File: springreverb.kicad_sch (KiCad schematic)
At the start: 53 parts, among them J1 IN, J10 From_Tank, J11 From2, J12 From, J13 VR2_3, J14 OUT, J2 GND2, J3 GND, J4 Vin, J5 VR1_3, J6 VR1_2, J7 To, J8 To2, J9 To_Tank, U1 TL072, U2 TC1044S, U3 4556ADD

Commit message: 配置修整
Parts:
- added R14, R15: 10, Resistor_THT:R_Axial_DIN0204_L3.6mm_D1.6mm_P7.62mm_Horizontal, symbol Device:R_Small
- J2: value GND2 -> VR1_1
- R10: value 10 -> 47
- R12: footprint Resistor_THT:R_Axial_DIN0204_L3.6mm_D1.6mm_P7.62mm_Horizontal -> Resistor_THT:R_Axial_DIN0204_L3.6mm_D1.6mm_P2.54mm_Vertical
- R7: value 10 -> 100
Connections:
- net GND: now also C1.1, C15.2, J10.2 (Ext), J11.1 (Pin_1), R11.2, R13.2, R2.2, VR3.3
- net at C8.2, J7.1 (Pin_1), J9.1 (In): now also R14.1, R15.1; no longer U3.1, U3.7
- net at C5.1, J5.1 (Pin_1), U1.1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: no longer VR1.3
- removed net GND2: C1.1, C15.2, J2.1 (Pin_1), R13.2, R2.2, VR3.3
- removed net GND3: J10.2 (Ext), J11.1 (Pin_1), R11.2, R5.1, VR1.1
- new net: R15.2, U3.7
- new net: R14.2, U3.1
- new net: J2.1 (Pin_1), R5.1, VR1.1
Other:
- note added: "入力線はシールド線で網線の基板側は接続しない 電源、GND2(回路)、GND3(タンク)はTL072の近く(3番ピンと6、7版番ピンの合流地点)で 合流させて一本でジャックのsleeveへ"
- moved on the sheet: C1, C2, C5, C8, J1, J10, J11, J12, J13, J5, J6, J7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

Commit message: 部品を配置した
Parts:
- added H1, H2, H3, H4: MountingHole, MountingHole:MountingHole_3.2mm_M3, symbol Mechanical:MountingHole
- added J16: VR2_3GND, MyLibrary:PinHeader_1x01_P2.54mm_Vertical, symbol Connector:Conn_01x01_Pin
- added J2: INGND, MyLibrary:PinHeader_1x01_P2.54mm_Vertical, symbol Connector:Conn_01x01_Pin
- added J8: ToGND, MyLibrary:PinHeader_1x01_P2.54mm_Vertical, symbol Connector:Conn_01x01_Pin
- C11, C14: value 25v100u -> 100u
- C3, C9: value 50v100u -> 1000u; footprint Capacitor_THT:CP_Radial_D7.5mm_P2.50mm -> Capacitor_THT:CP_Radial_D10.0mm_P5.00mm
- J13: renamed from J11; value From2 -> FromGND
- renumbered C8 to C6, C6 to C7, C7 to C8, J8 to J10, J9 to J11, J10 to J12, J12 to J14, J13 to J15, J14 to J17, J2 to J6, J6 to J7, J7 to J9, R8 to R10, R9 to R11, R10 to R12, R11 to R13, R12 to R14, R13 to R15, R15 to R6, R14 to R7, R6 to R8, R7 to R9
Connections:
- net GND: now also J16.1 (Pin_1), J2.1 (Pin_1), J8.1 (Pin_1)
- net at C5.1, J5.1 (Pin_1), U1.1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: now also VR1.3
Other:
- note added: "入力線はシールド線でだけど網線は片側接地 電源、GND2(回路)、GND3(タンク)はTL072の近く(3番ピンと6、7版番ピンの合流地点)で 合流させて一本でジャックのsleeveへ 入力は基板に片側接地 VR1は3本シールド線でケースに片側接地 VR2_3は基板で片側接地"
- note removed: "入力線はシールド線で網線の基板側は接続しない 電源、GND2(回路)、GND3(タンク)はTL072の近く(3番ピンと6、7版番ピンの合流地点)で 合流させて一本でジャックのsleeveへ"

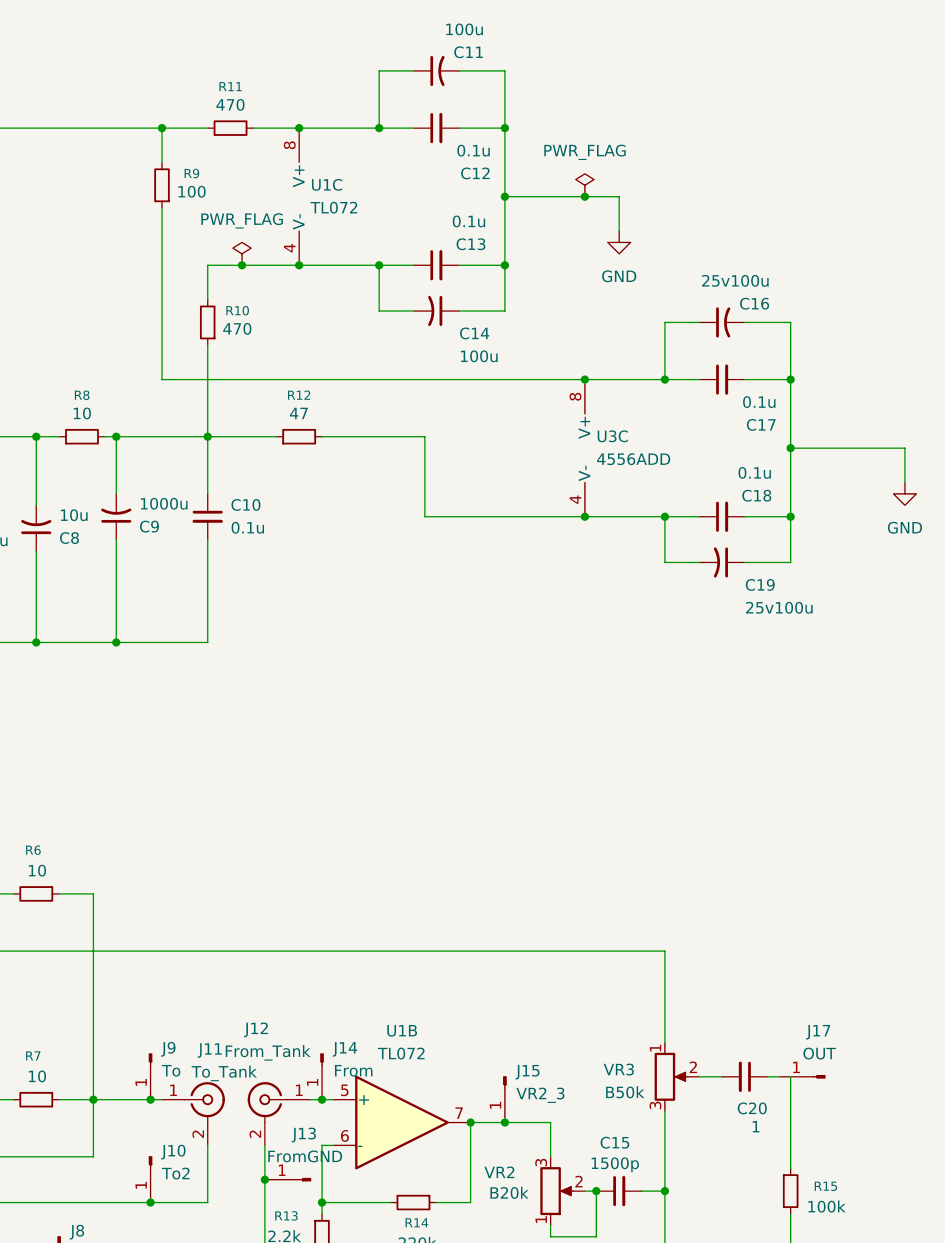
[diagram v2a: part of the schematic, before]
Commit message: フラグを追加
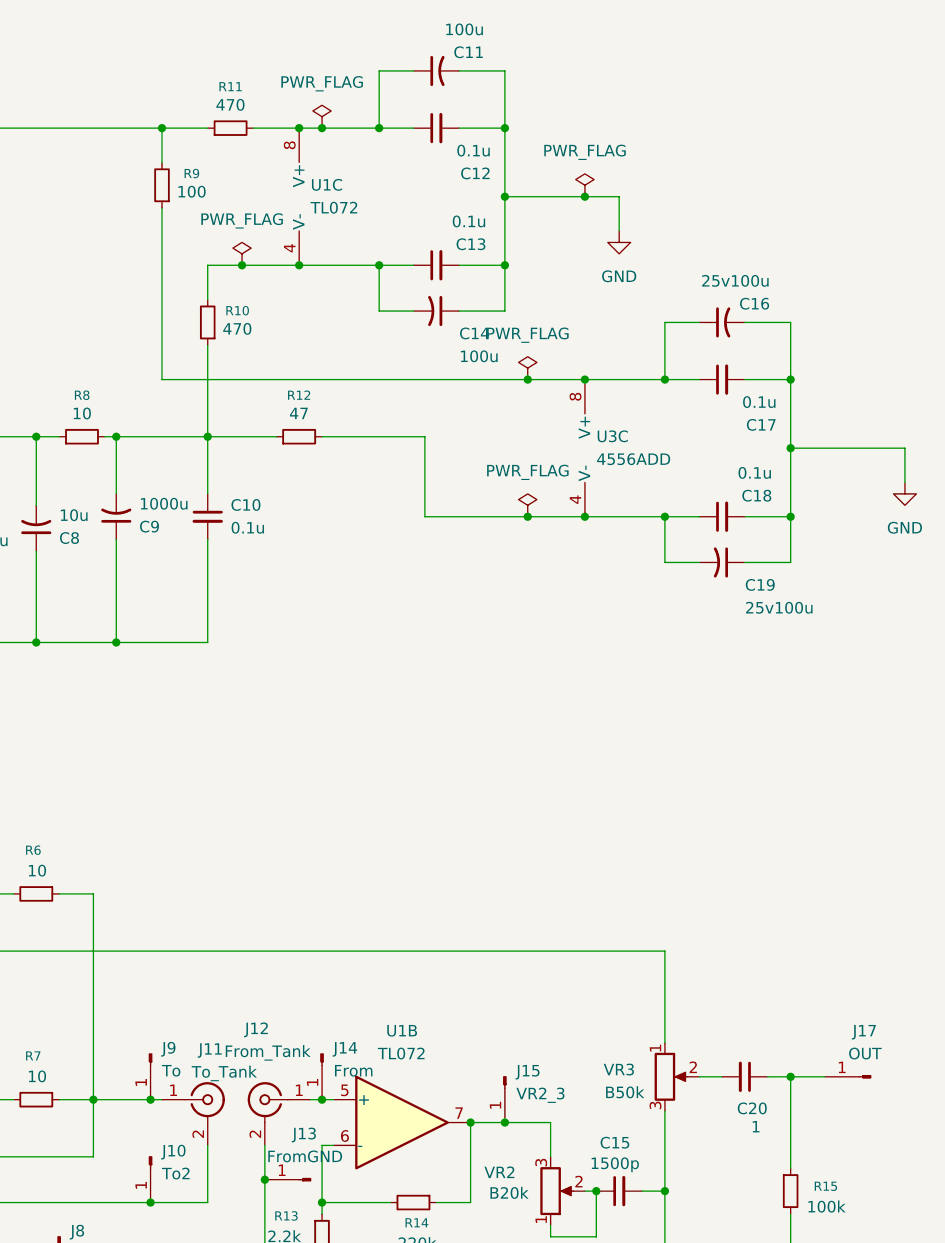
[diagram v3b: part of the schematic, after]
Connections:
- net at C20.1, J17.1 (Pin_1): now also R15.1
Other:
- moved on the sheet: J17

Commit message: 表示の修正
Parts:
- C16, C19: value 25v100u -> 100u
- C2: value 0.1 -> 0.1u
- C20: value 1 -> 1u
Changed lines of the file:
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@@
 		(dnp no)
 		(property "Reference" "C14"
-			(at 161.29 57.15 90)
+			(at 157.988 57.404 90)
 			(effects
 				(font
@@
 		)
 		(property "Value" "100u"
-			(at 161.29 59.69 90)
+			(at 158.242 59.69 90)
 			(effects
 				(font
@@
 			)
 		)
-		(property "Value" "1"
+		(property "Value" "1u"
 			(at 194.818 145.288 90)
 			(effects
@@
 			)
 		)
-		(property "Value" "25v100u"
+		(property "Value" "100u"
 			(at 195.834 51.308 90)
 			(effects
@@
 			)
 		)
-		(property "Value" "25v100u"
+		(property "Value" "100u"
 			(at 193.04 87.63 90)
 			(effects
@@
 			)
 		)
-		(property "Value" "0.1"
-			(at 39.624 127.762 90)
+		(property "Value" "0.1u"
+			(at 40.64 127.762 90)
 			(effects
 				(font

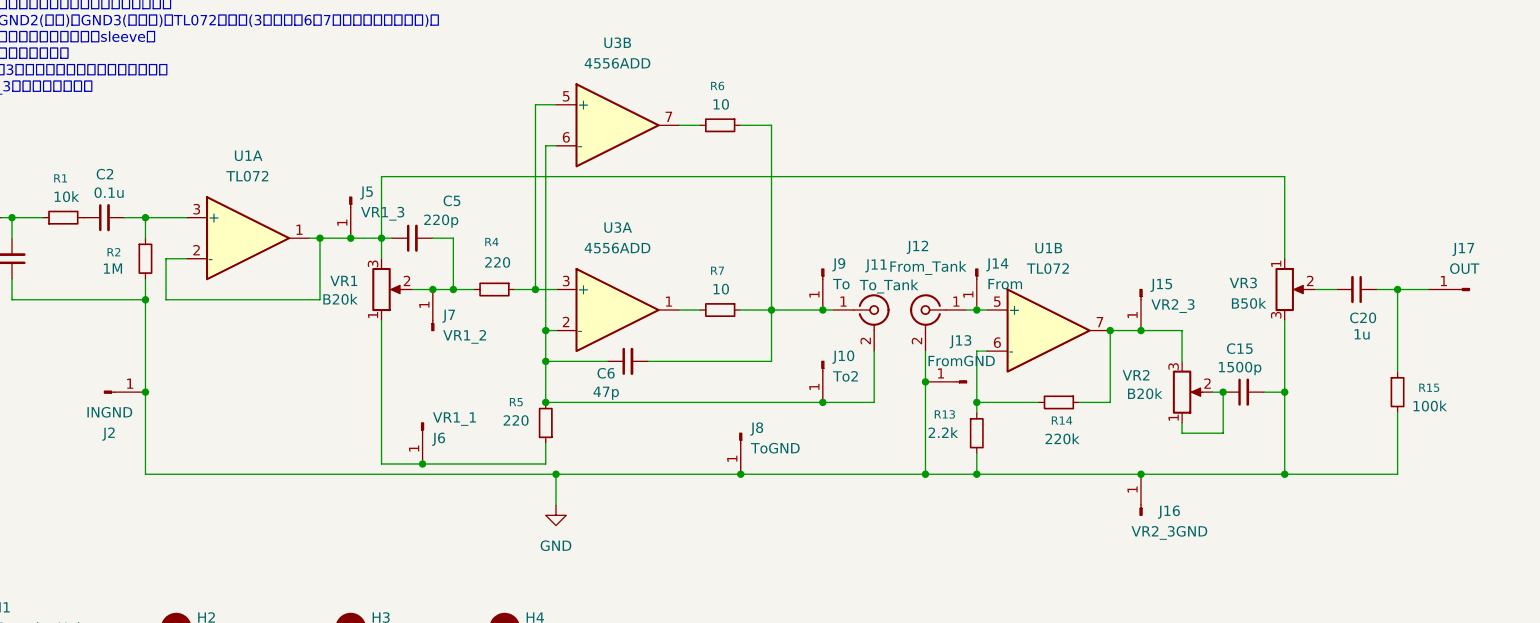
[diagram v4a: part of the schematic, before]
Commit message: ボリュームのつなぎ方とか色々修正
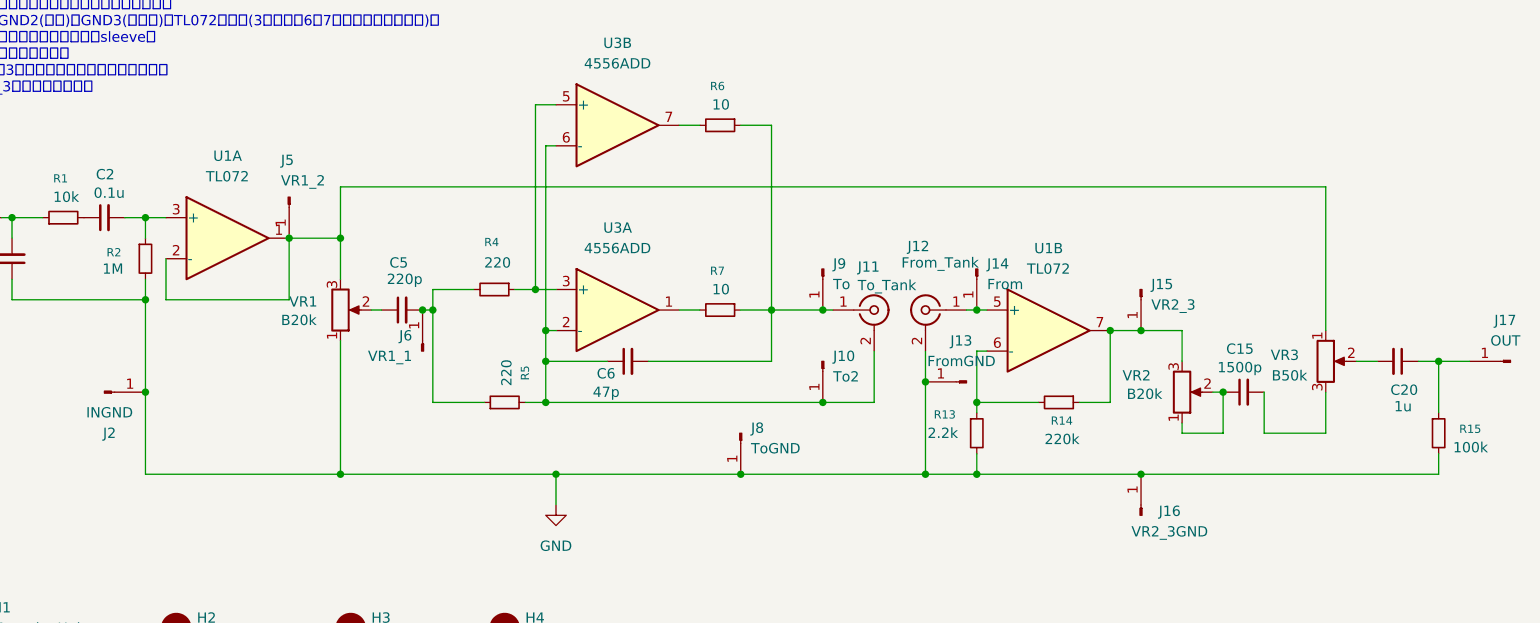
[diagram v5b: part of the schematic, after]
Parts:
- removed J7: VR1_2, MyLibrary:PinHeader_1x01_P2.54mm_Vertical, symbol Connector:Conn_01x01_Pin
- J5: value VR1_3 -> VR1_2
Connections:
- net GND: now also VR1.1; no longer C15.2, VR3.3
- net at C5.2, R4.2: now also J6.1 (Pin_1), R5.1; no longer VR1.2
- net at J5.1 (Pin_1), U1.1, U1.2 (-)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: no longer C5.1
- new net: C15.2, VR3.3
- new net: C5.1, VR1.2
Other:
- moved on the sheet: C20, C5, J17, J5, J6, R15, R5, U1A, VR1, VR3

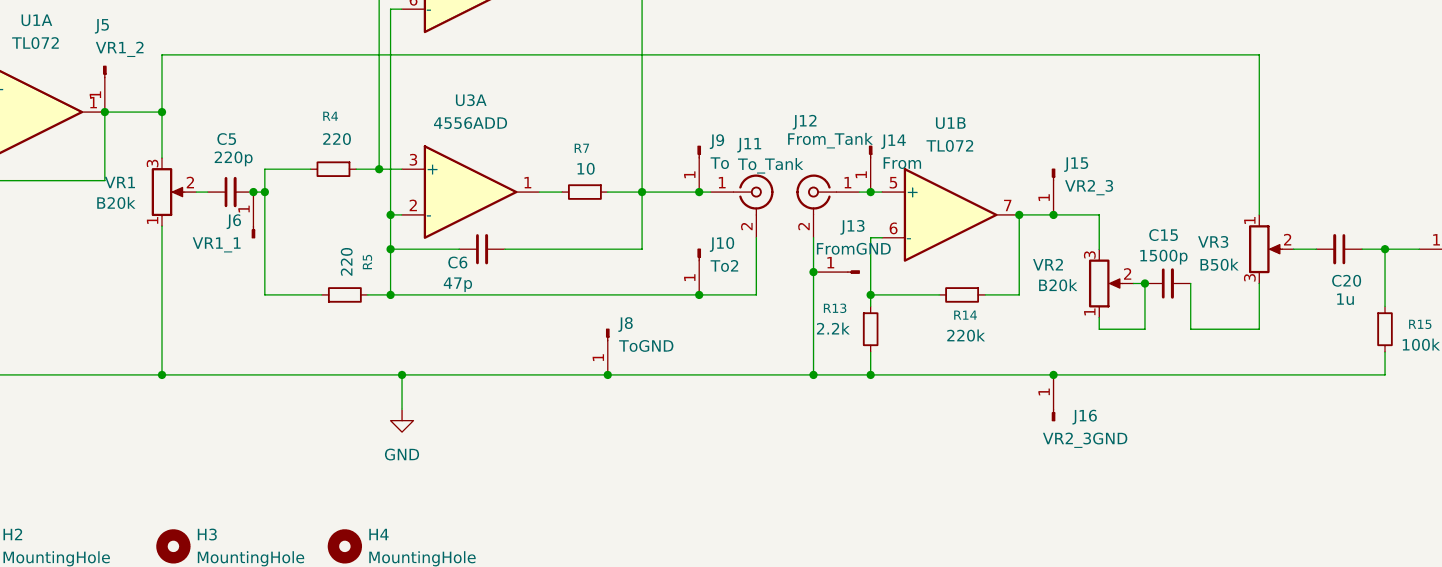
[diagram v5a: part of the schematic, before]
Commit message: ドライブ段の回路がおかしかった
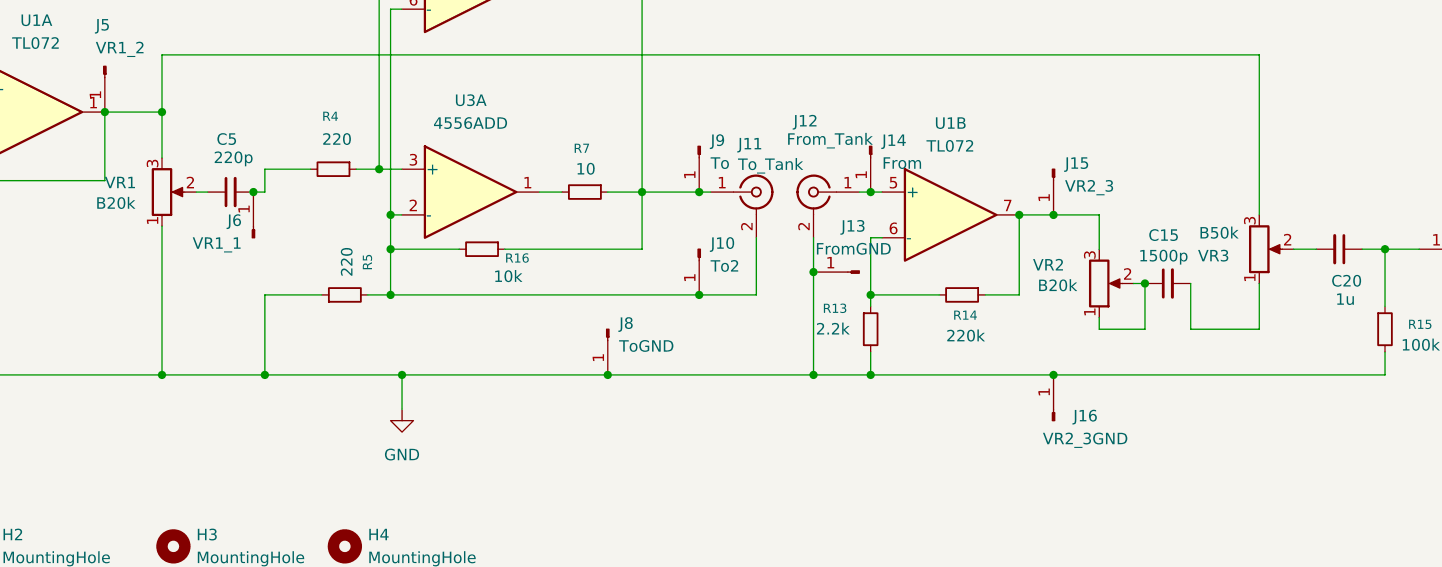
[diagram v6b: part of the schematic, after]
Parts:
- removed C6: 47p, Capacitor_THT:C_Disc_D3.0mm_W1.6mm_P2.50mm, symbol Device:C_Small
- added R16: 10k, Resistor_THT:R_Axial_DIN0204_L3.6mm_D1.6mm_P7.62mm_Horizontal, symbol Device:R_Small
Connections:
- net GND: now also R5.1
- net at C5.2, J6.1 (Pin_1), R4.2: no longer R5.1
- net at J10.1 (Pin_1), J11.2 (Ext), R5.2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: now also R16.2
- net at J5.1 (Pin_1), U1.1, U1.2 (-)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: now also VR3.3; no longer VR3.1
- net at C15.2: now also VR3.1; no longer VR3.3
- net at J11.1 (In), J9.1 (Pin_1), R6.1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: now also R16.1
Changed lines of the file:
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@@
 	)
 	(junction
-		(at 78.74 142.24)
-		(diameter 0)
-		(color 0 0 0 0)
-	)
-	(junction
 		(at 123.19 68.58)
 		(diameter 0)
@@
 		(color 0 0 0 0)
 	)
+	(junction
+		(at 78.74 162.56)
+		(diameter 0)
+		(color 0 0 0 0)
+	)
 	(wire
 		(pts
@@
 	(wire
 		(pts
+			(xy 78.74 153.67) (xy 78.74 162.56)
+		)
+		(stroke
+			(width 0)
+			(type default)
+		)
+	)
+	(wire
+		(pts
 			(xy 168.91 77.47) (xy 175.26 77.47)
 		)
@@
 	(wire
 		(pts
-			(xy 67.31 162.56) (xy 93.98 162.56)
+			(xy 67.31 162.56) (xy 78.74 162.56)
 		)
 		(stroke
@@
 	(wire
 		(pts
-			(xy 78.74 153.67) (xy 78.74 142.24)
-		)
-		(stroke
-			(width 0)
-			(type default)
-		)
-	)
-	(wire
-		(pts
 			(xy 67.31 127) (xy 67.31 133.35)
 		)
@@
 	(wire
 		(pts
+			(xy 78.74 162.56) (xy 93.98 162.56)
+		)
+		(stroke
+			(width 0)
+			(type default)
+		)
+	)
+	(wire
+		(pts
 			(xy 26.67 138.43) (xy 26.67 140.97)
 		)
@@
 		(lib_id "Device:R_Potentiometer")
 		(at 189.23 148.59 0)
+		(mirror x)
 		(unit 1)
 		(exclude_from_sim no)
@@
 		(dnp no)
 		(property "Reference" "VR3"
-			(at 185.928 147.828 0)
+			(at 185.928 149.352 0)
 			(effects
 				(font
@@
 		)
 		(property "Value" "B50k"
-			(at 186.944 150.368 0)
+			(at 186.944 146.812 0)
 			(effects
 				(font
@@
 	)
 	(symbol
-		(lib_id "Device:C_Small")
-		(at 102.87 148.59 90)
-		(unit 1)
-		(exclude_from_sim no)
-		(in_bom yes)
-		(on_board yes)
-		(dnp no)
-		(property "Reference" "C6"
-			(at 101.346 150.114 90)
-			(effects
-				(font
-					(size 1.27 1.27)
-				)
-				(justify left)
-			)
-		)
-		(property "Value" "47p"
-			(at 101.854 152.4 90)
-			(effects
-				(font
-					(size 1.27 1.27)
-				)
-				(justify left)
-			)
-		)
-		(property "Footprint" "Capacitor_THT:C_Disc_D3.0mm_W1.6mm_P2.50mm"
-			(at 102.87 148.59 0)
-			(effects
-				(font
-					(size 1.27 1.27)
-				)
-				(hide yes)
-			)
-		)
-		(property "Datasheet" "~"
-			(at 102.87 148.59 0)
-			(effects
-				(font
-					(size 1.27 1.27)
-				)
-				(hide yes)
-			)
-		)
-		(property "Description" "Unpolarized capacitor, small symbol"
-			(at 102.87 148.59 0)
-			(effects
-				(font
-					(size 1.27 1.27)
-				)
-				(hide yes)
-			)
-		)
-		(pin "2"
-		)
-		(pin "1"
-		)
-		(instances
-			(project "springreverb"
-				(path "/db334565-2b42-4a43-9204-0bb0e555e376"
-					(reference "C6")
-					(unit 1)
-				)
-			)
-		)
-	)
-	(symbol
 		(lib_id "Device:C_Small_US")
 		(at 123.19 77.47 0)
@@
 					(unit 1)
 				)
+			)
+		)
+	)
+	(symbol
+		(lib_id "Device:R_Small")
+		(at 102.87 148.59 270)
+		(unit 1)
+		(exclude_from_sim no)
+		(in_bom yes)
+		(on_board yes)
+		(dnp no)
+		(property "Reference" "R16"
+			(at 105.41 149.606 90)
+			(effects
+				(font
+					(size 1.016 1.016)
+				)
+				(justify left)
+			)
+		)
+		(property "Value" "10k"
+			(at 104.14 151.638 90)
+			(effects
+				(font
+					(size 1.27 1.27)
+				)
+				(justify left)
+			)
+		)
+		(property "Footprint" "Resistor_THT:R_Axial_DIN0204_L3.6mm_D1.6mm_P7.62mm_Horizontal"
+			(at 102.87 148.59 0)
+			(effects
+				(font
+					(size 1.27 1.27)
+				)
+				(hide yes)
+			)
+		)
+		(property "Datasheet" "~"
+			(at 102.87 148.59 0)
+			(effects
+				(font
+					(size 1.27 1.27)
+				)
+				(hide yes)
+			)
+		)
+		(property "Description" "Resistor, small symbol"
+			(at 102.87 148.59 0)
+			(effects
+				(font
+					(size 1.27 1.27)
+				)
+				(hide yes)
+			)
+		)
+		(pin "1"
+		)
+		(pin "2"
+		)
+		(instances
+			(project "springreverb"
+				(path "/db334565-2b42-4a43-9204-0bb0e555e376"
+					(reference "R16")
+					(unit 1)
+				)
